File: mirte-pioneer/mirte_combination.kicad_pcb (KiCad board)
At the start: 2 copper layers, 55.6 x 81.9 mm, 50 parts, among them J1 Servo3, J10 IR1, J11 Conn_01x13_Female, J12 IR Object Detector 1, J14 IR2, J17 MC1, J18 MC2, J19 Servo1, J2 Conn_01x20_Female, J20 SRF1, J21 ENC2, J23 MC1-A, J24 MC1-B, J25 SRF2, J26 ENC1, J27 Servo2, J28 I2C2, J3 Servo4, J30 I2C1, J33 line out left, J35 Power out, J37 on/off, J4 Conn_01x20_Female, J5 Conn_01x06_Pin, J7 Keypad, J8 Conn_01x06_Female, J9 IR Object Detector 2, Q1 DMG2305UX, Q2 DMN2050L, SW2 SK12D07VG5, U2 CH340E

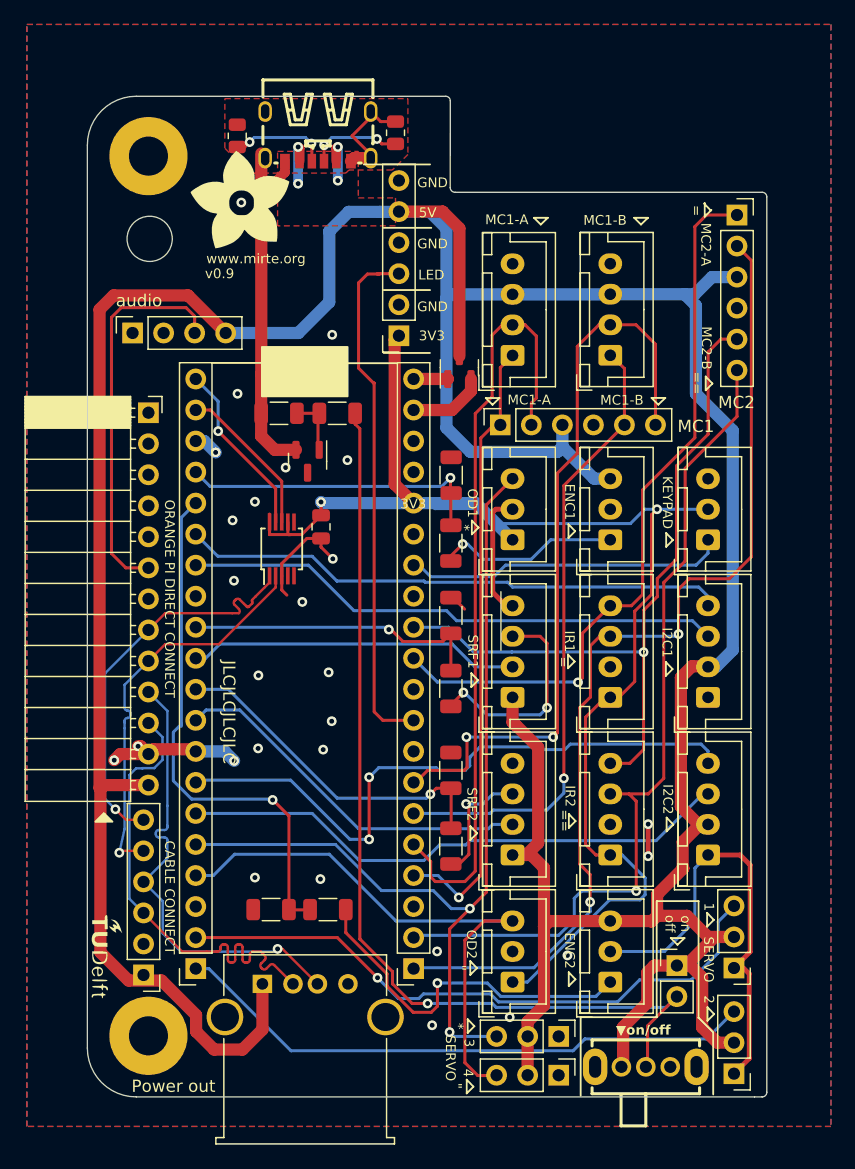
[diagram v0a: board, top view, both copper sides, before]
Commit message: usb b micro instead of c for v0.9
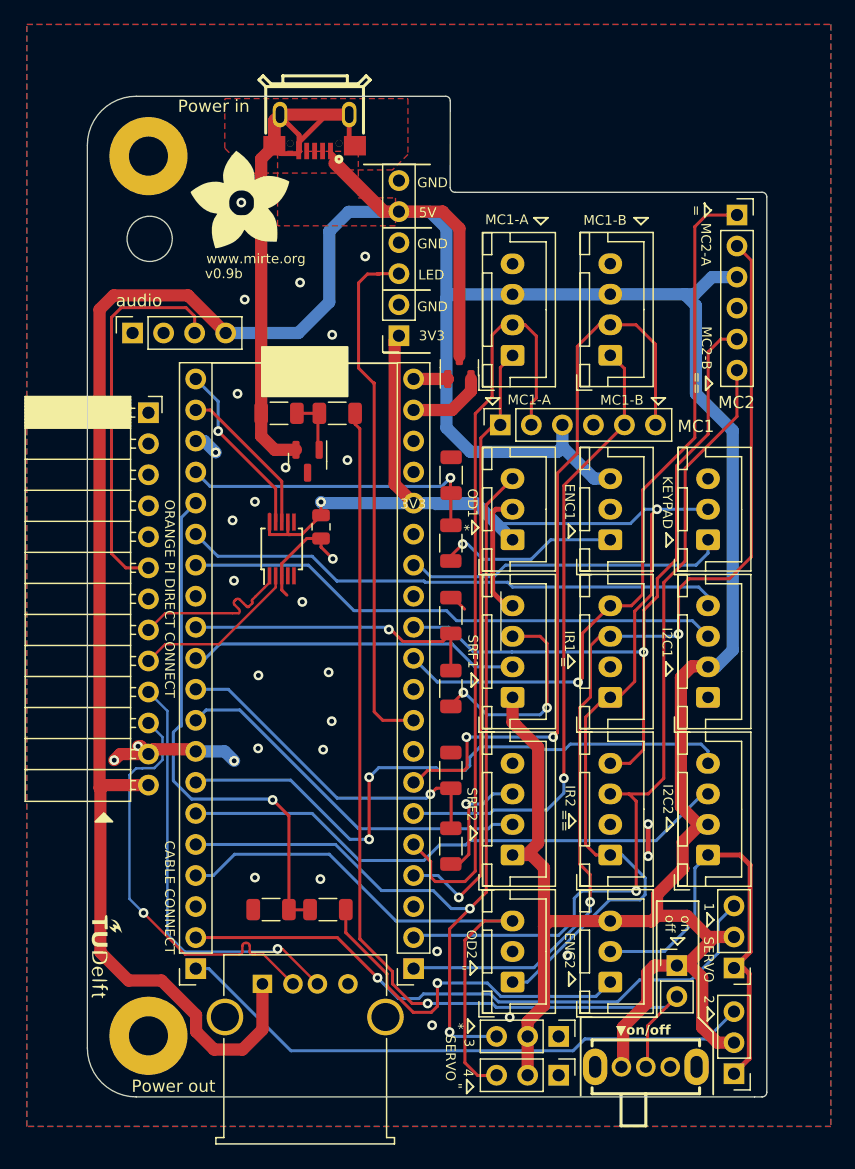
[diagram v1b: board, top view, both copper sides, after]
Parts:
- removed J5: Conn_01x06_Pin, Connector_PinHeader_2.54mm:PinHeader_1x06_P2.54mm_Vertical
- removed R1, R12: 5k1, Resistor_SMD:R_0805_2012Metric
- removed USB1: TYPE-C 6P(073), lcsc:TYPE-C-SMD_TYPE-C-6P_5
- added USB2: U254-051T-4BH83-S1S, lcsc:MICRO-USB-SMD_U254-051T-4BH83-S1S, F.Cu at (118.6, 53.1)
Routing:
- net GND: track 39.1 -> 75.2 mm
- net D+: track 33.1 -> 13.9 mm, vias 1 -> 0
- net D-: track 33.0 -> 13.9 mm, vias 1 -> 0
- net Net-(USB1-CC2): track 8.05 -> 0.00 mm, vias 2 -> 0
- net Net-(USB1-CC1): track 7.63 -> 0.00 mm, vias 2 -> 0
- net 5V: track 335.5 -> 341.8 mm, vias 4 -> 0
- net usb-d2-: track 39.3 -> 34.6 mm, vias 0 -> 1
- net usb-d2+: track 37.9 -> 34.6 mm
- net D_GND: vias 27 -> 30
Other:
- board text added: "Power in"
- board text added: "v0.9b"
- board text removed: "JLCJLCJLCJLC"
- board text removed: "v0.9"
